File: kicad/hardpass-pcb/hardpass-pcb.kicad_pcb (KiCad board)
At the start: 2 copper layers, 80 x 65 mm, 59 parts, among them P1 Pi_Zero, P2 OLED_I2C, P3 Pi_Zero, SW1 1, SW10 C/UP, SW11 0/OK, SW12 OK/DN, SW2 2, SW3 3, SW4 4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

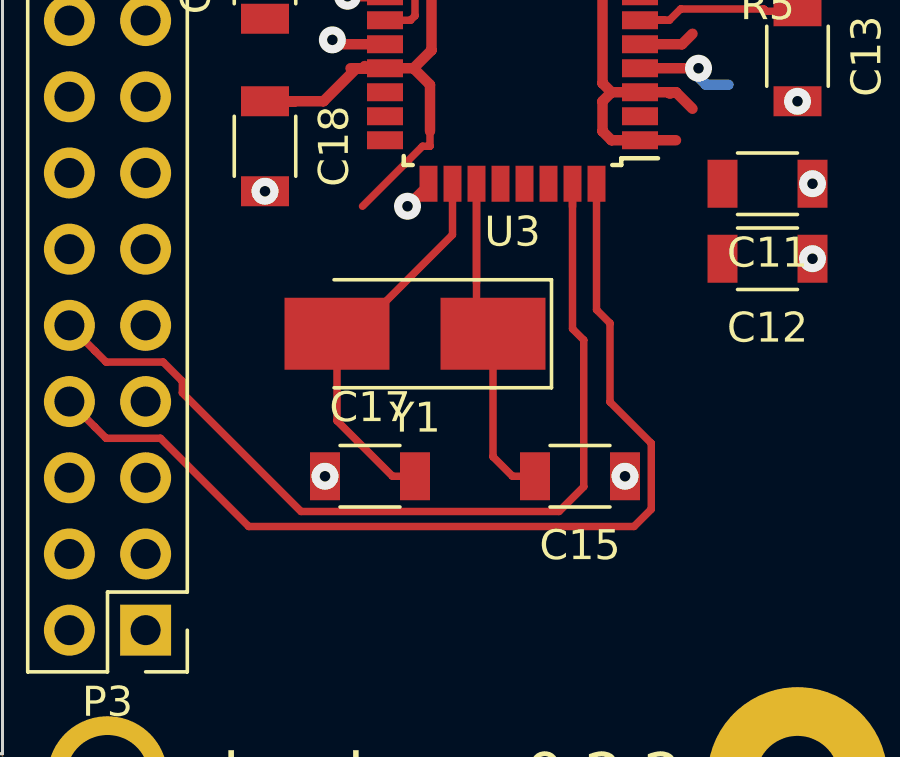
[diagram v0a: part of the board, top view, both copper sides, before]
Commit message: cleanup tracks around xtal
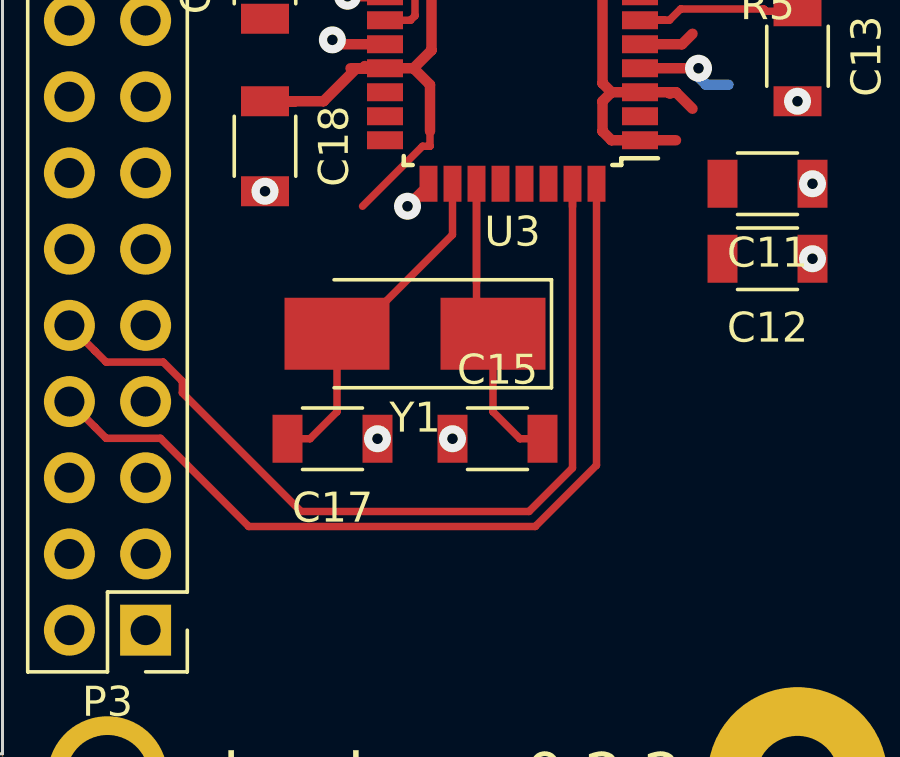
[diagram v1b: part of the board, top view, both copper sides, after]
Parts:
- moved C15 3.02 mm to (66.5, 50.2), turned to 0 degrees
- moved C17 1.77 mm to (61.0, 50.2), turned to 180 degrees
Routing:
- net CARD_RX: track 33.0 -> 29.5 mm
- net Net-(C17-Pad2): track 13.2 -> 11.5 mm
- net Net-(C15-Pad2): track 14.3 -> 13.2 mm
- net CARD_TX: track 31.3 -> 30.4 mm
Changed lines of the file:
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@@
     (links 167)
     (no_connects 8)
-    (area -0.050001 -0.050001 80.050001 65.050001)
+    (area -0.666014 -0.573 80.050001 65.655)
     (thickness 1.6)
     (drawings 26)
-    (tracks 724)
+    (tracks 718)
     (zones 0)
     (modules 59)
@@
   )
   (module Capacitors_SMD:C_1206 (layer F.Cu)
-    (at 69.25 51.5 180)
+    (at 66.5 50.25)
     (descr "Capacitor SMD 1206, reflow soldering, AVX (see smccp.pdf)")
     (tags "capacitor 1206")
     (attr smd)
-    (fp_text reference C15 (at 0 -2.3 180) (layer F.SilkS)
+    (fp_text reference C15 (at 0 -2.3) (layer F.SilkS)
       (effects (font (size 1 1) (thickness 0.15)))
     )
-    (fp_text value 22pF (at 0 2.3 180) (layer F.Fab)
+    (fp_text value 22pF (at 0 2.3) (layer F.Fab)
       (effects (font (size 1 1) (thickness 0.15)))
     )
@@
     (fp_line (start 1 -1.025) (end -1 -1.025) (layer F.SilkS) (width 0.12))
     (fp_line (start -1 1.025) (end 1 1.025) (layer F.SilkS) (width 0.12))
-    (pad 1 smd rect (at -1.5 0 180) (size 1 1.6) (layers F.Cu F.Paste F.Mask)
+    (pad 1 smd rect (at -1.5 0) (size 1 1.6) (layers F.Cu F.Paste F.Mask)
       (net 1 GND))
-    (pad 2 smd rect (at 1.5 0 180) (size 1 1.6) (layers F.Cu F.Paste F.Mask)
+    (pad 2 smd rect (at 1.5 0) (size 1 1.6) (layers F.Cu F.Paste F.Mask)
       (net 72 "Net-(C15-Pad2)"))
     (model Capacitors_SMD.3dshapes/C_1206.wrl
@@
   )
   (module Capacitors_SMD:C_1206 (layer F.Cu)
-    (at 62.25 51.5)
+    (at 61 50.25 180)
     (descr "Capacitor SMD 1206, reflow soldering, AVX (see smccp.pdf)")
     (tags "capacitor 1206")
     (attr smd)
-    (fp_text reference C17 (at 0 -2.3) (layer F.SilkS)
+    (fp_text reference C17 (at 0 -2.3 180) (layer F.SilkS)
       (effects (font (size 1 1) (thickness 0.15)))
     )
-    (fp_text value 22pF (at 0 2.3) (layer F.Fab)
+    (fp_text value 22pF (at 0 2.3 180) (layer F.Fab)
       (effects (font (size 1 1) (thickness 0.15)))
     )
@@
     (fp_line (start 1 -1.025) (end -1 -1.025) (layer F.SilkS) (width 0.12))
     (fp_line (start -1 1.025) (end 1 1.025) (layer F.SilkS) (width 0.12))
-    (pad 1 smd rect (at -1.5 0) (size 1 1.6) (layers F.Cu F.Paste F.Mask)
+    (pad 1 smd rect (at -1.5 0 180) (size 1 1.6) (layers F.Cu F.Paste F.Mask)
       (net 1 GND))
-    (pad 2 smd rect (at 1.5 0) (size 1 1.6) (layers F.Cu F.Paste F.Mask)
+    (pad 2 smd rect (at 1.5 0 180) (size 1 1.6) (layers F.Cu F.Paste F.Mask)
       (net 74 "Net-(C17-Pad2)"))
     (model Capacitors_SMD.3dshapes/C_1206.wrl
@@
   (via (at 71 32) (size 0.9) (drill 0.35) (layers F.Cu B.Cu) (net 1))
   (via (at 70.5 30.25) (size 0.9) (drill 0.35) (layers F.Cu B.Cu) (net 1))
-  (via (at 70.75 51.5) (size 0.9) (drill 0.35) (layers F.Cu B.Cu) (net 1))
-  (via (at 60.75 51.5) (size 0.9) (drill 0.35) (layers F.Cu B.Cu) (net 1))
+  (via (at 65 50.25) (size 0.9) (drill 0.35) (layers F.Cu B.Cu) (net 1))
+  (via (at 62.5 50.25) (size 0.9) (drill 0.35) (layers F.Cu B.Cu) (net 1))
   (via (at 73.2 37.9) (size 0.9) (drill 0.35) (layers F.Cu B.Cu) (net 1))
   (segment (start 62.75 37.1) (end 61.142188 37.1) (width 0.35) (layer F.Cu) (net 1))
@@
   (segment (start 75.45 36) (end 76.5 36) (width 0.25) (layer F.Cu) (net 71))
   (segment (start 72.1 36.3) (end 71.25 36.3) (width 0.25) (layer F.Cu) (net 71))
-  (segment (start 66.35 46.75) (end 66.35 50.85) (width 0.25) (layer F.Cu) (net 72))
-  (segment (start 66.35 50.85) (end 67 51.5) (width 0.25) (layer F.Cu) (net 72))
-  (segment (start 67 51.5) (end 67.75 51.5) (width 0.25) (layer F.Cu) (net 72))
+  (segment (start 66.35 46.75) (end 66.35 49.35) (width 0.25) (layer F.Cu) (net 72))
+  (segment (start 67.25 50.25) (end 68 50.25) (width 0.25) (layer F.Cu) (net 72))
+  (segment (start 66.35 49.35) (end 67.25 50.25) (width 0.25) (layer F.Cu) (net 72))
   (segment (start 65.8 41.75) (end 65.8 46.2) (width 0.25) (layer F.Cu) (net 72))
   (segment (start 65.8 46.2) (end 66.35 46.75) (width 0.25) (layer F.Cu) (net 72))
   (segment (start 65.8 41.75) (end 65.8 45.05) (width 0.25) (layer F.Cu) (net 72))
-  (segment (start 61.15 46.75) (end 61.15 49.65) (width 0.25) (layer F.Cu) (net 74))
-  (segment (start 61.15 49.65) (end 63 51.5) (width 0.25) (layer F.Cu) (net 74))
-  (segment (start 63 51.5) (end 63.75 51.5) (width 0.25) (layer F.Cu) (net 74))
+  (segment (start 61.15 46.75) (end 61.15 49.35) (width 0.25) (layer F.Cu) (net 74))
+  (segment (start 61.15 49.35) (end 60.25 50.25) (width 0.25) (layer F.Cu) (net 74))
+  (segment (start 60.25 50.25) (end 59.5 50.25) (width 0.25) (layer F.Cu) (net 74))
   (segment (start 65 41.75) (end 65 43.45) (width 0.25) (layer F.Cu) (net 74))
   (segment (start 61.7 46.75) (end 61.15 46.75) (width 0.25) (layer F.Cu) (net 74))
@@
   (segment (start 72.1 35.5) (end 71.25 35.5) (width 0.25) (layer F.Cu) (net 81))
   (segment (start 72.574999 35.375001) (end 72.224999 35.375001) (width 0.25) (layer F.Cu) (net 81))
-  (segment (start 69 41.75) (end 69 46.584998) (width 0.25) (layer F.Cu) (net 91))
-  (segment (start 69.375001 46.959999) (end 69.375001 51.850001) (width 0.25) (layer F.Cu) (net 91))
-  (segment (start 69 46.584998) (end 69.375001 46.959999) (width 0.25) (layer F.Cu) (net 91))
-  (segment (start 69.375001 51.850001) (end 68.550001 52.675001) (width 0.25) (layer F.Cu) (net 91))
-  (segment (start 68.550001 52.675001) (end 59.949999 52.675001) (width 0.25) (layer F.Cu) (net 91))
+  (segment (start 69 41.75) (end 69 51.225002) (width 0.25) (layer F.Cu) (net 91))
+  (segment (start 69 51.225002) (end 67.550001 52.675001) (width 0.25) (layer F.Cu) (net 91))
   (segment (start 59.949999 52.675001) (end 55.995001 48.720003) (width 0.25) (layer F.Cu) (net 91))
-  (segment (start 53.455001 47.695001) (end 53.079999 47.319999) (width 0.25) (layer F.Cu) (net 91))
+  (segment (start 67.550001 52.675001) (end 59.949999 52.675001) (width 0.25) (layer F.Cu) (net 91))
   (segment (start 55.995001 48.720003) (end 55.995001 48.332001) (width 0.25) (layer F.Cu) (net 91))
   (segment (start 55.995001 48.332001) (end 55.358001 47.695001) (width 0.25) (layer F.Cu) (net 91))
+  (segment (start 53.455001 47.695001) (end 53.079999 47.319999) (width 0.25) (layer F.Cu) (net 91))
   (segment (start 55.358001 47.695001) (end 53.455001 47.695001) (width 0.25) (layer F.Cu) (net 91))
   (segment (start 53.079999 47.319999) (end 52.23 46.47) (width 0.25) (layer F.Cu) (net 91))
   (segment (start 69 41.75) (end 69 42.525002) (width 0.25) (layer F.Cu) (net 91))
-  (segment (start 69.8 41.75) (end 69.8 45.95) (width 0.25) (layer F.Cu) (net 92))
-  (segment (start 71.625001 50.399999) (end 71.625001 52.600001) (width 0.25) (layer F.Cu) (net 92))
+  (segment (start 69.8 41.75) (end 69.8 51.132122) (width 0.25) (layer F.Cu) (net 92))
   (segment (start 58.208013 53.175011) (end 55.268003 50.235001) (width 0.25) (layer F.Cu) (net 92))
+  (segment (start 69.8 51.132122) (end 67.757111 53.175011) (width 0.25) (layer F.Cu) (net 92))
+  (segment (start 67.757111 53.175011) (end 58.208013 53.175011) (width 0.25) (layer F.Cu) (net 92))
   (segment (start 55.268003 50.235001) (end 53.455001 50.235001) (width 0.25) (layer F.Cu) (net 92))
-  (segment (start 69.8 45.95) (end 70.25 46.4) (width 0.25) (layer F.Cu) (net 92))
   (segment (start 53.455001 50.235001) (end 53.079999 49.859999) (width 0.25) (layer F.Cu) (net 92))
-  (segment (start 70.25 46.4) (end 70.25 49.024998) (width 0.25) (layer F.Cu) (net 92))
-  (segment (start 70.25 49.024998) (end 71.625001 50.399999) (width 0.25) (layer F.Cu) (net 92))
-  (segment (start 71.625001 52.600001) (end 71.049991 53.175011) (width 0.25) (layer F.Cu) (net 92))
-  (segment (start 71.049991 53.175011) (end 58.208013 53.175011) (width 0.25) (layer F.Cu) (net 92))
   (segment (start 53.079999 49.859999) (end 52.23 49.01) (width 0.25) (layer F.Cu) (net 92))
   (segment (start 70.45 27.25) (end 70.45 27.65) (width 0.25) (layer F.Cu) (net 121))

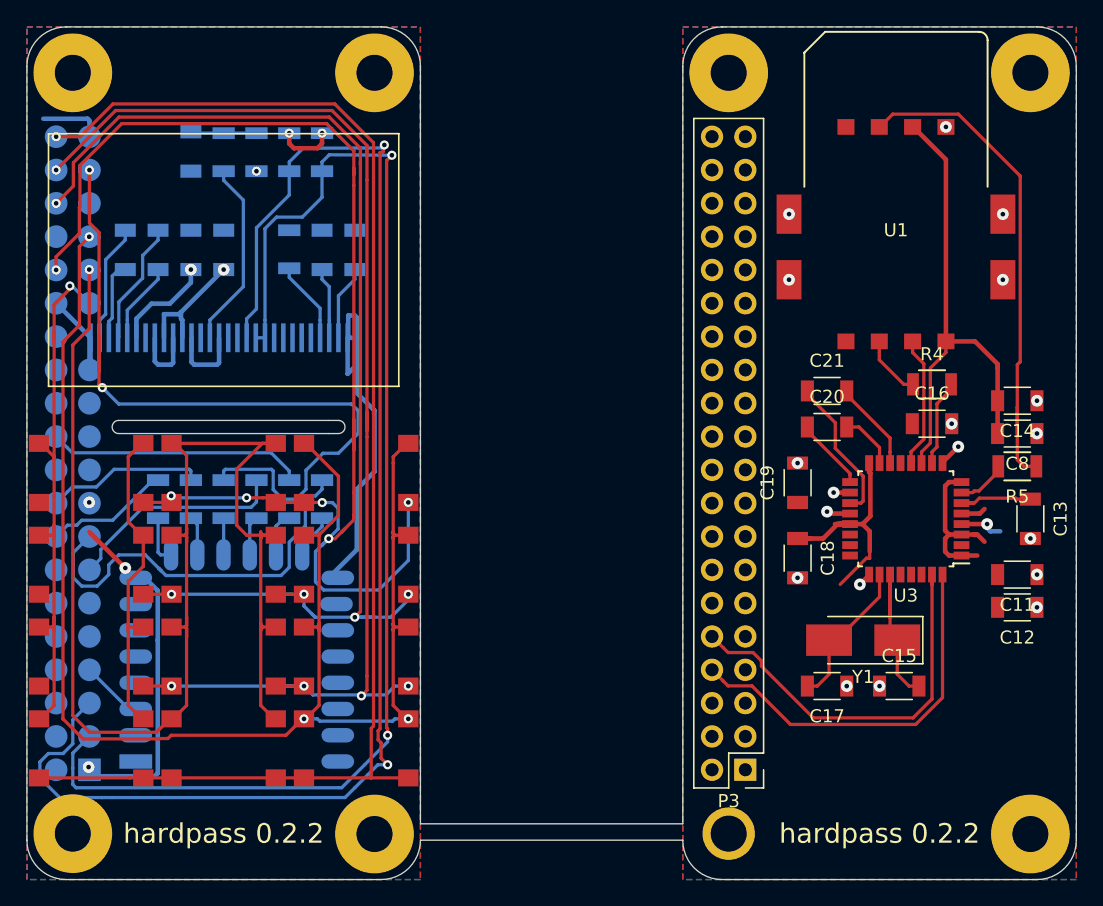
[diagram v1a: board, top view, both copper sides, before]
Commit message: fixed multiple things, add gnu logo
fixed:
 * mounting holes now non plated
 * fixed a few wires here and there
 * added a gnu/gpl logo for testing graphics
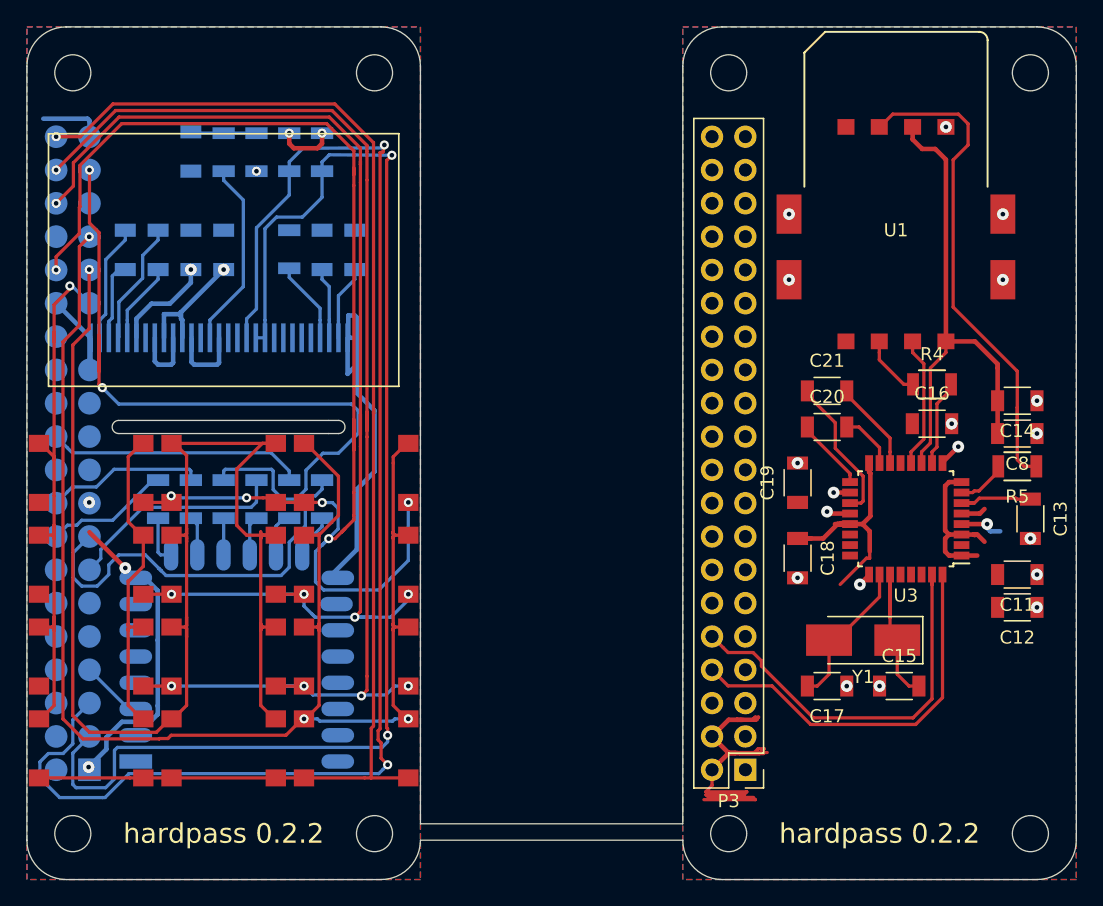
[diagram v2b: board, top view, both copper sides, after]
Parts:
- removed the REF** at (76.5, 61.5)
- removed the REF** at (76.5, 3.50)
- removed the REF** at (53.5, 3.50)
- removed the REF** at (53.5, 61.5)
- removed the REF** at (26.5, 61.5)
- removed the REF** at (3.50, 61.5)
- removed the REF** at (26.5, 3.50)
- removed the REF** at (3.50, 3.50)
- added ?: , RPi_Hat:RPi_Hat_Mounting_Hole, F.Cu at (53.5, 61.5)
- added ?: , RPi_Hat:RPi_Hat_Mounting_Hole, F.Cu at (76.5, 61.5)
- added ?: , RPi_Hat:RPi_Hat_Mounting_Hole, F.Cu at (76.5, 3.50)
- added ?: , RPi_Hat:RPi_Hat_Mounting_Hole, F.Cu at (53.5, 3.50)
- added ?: , RPi_Hat:RPi_Hat_Mounting_Hole, F.Cu at (26.5, 3.50)
- added ?: , RPi_Hat:RPi_Hat_Mounting_Hole, F.Cu at (26.5, 61.5)
- added ?: , RPi_Hat:RPi_Hat_Mounting_Hole, F.Cu at (3.50, 61.5)
- added ?: , RPi_Hat:RPi_Hat_Mounting_Hole, F.Cu at (3.50, 3.50)
- added REF**: Symbol_GNU-Logo_MaskTop, hardpass:Symbol_GNU-Logo_MaskTop, B.Cu at (65.0, 21.2)
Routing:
- net +5V: track 33.4 -> 73.8 mm
- net +3V3: track 49.4 -> 46.8 mm
- net OLED_SDA: track 97.4 -> 98.6 mm
- net Net-(R5-Pad1): track 38.5 -> 39.2 mm
- net Net-(C14-Pad2): track 37.4 -> 38.0 mm

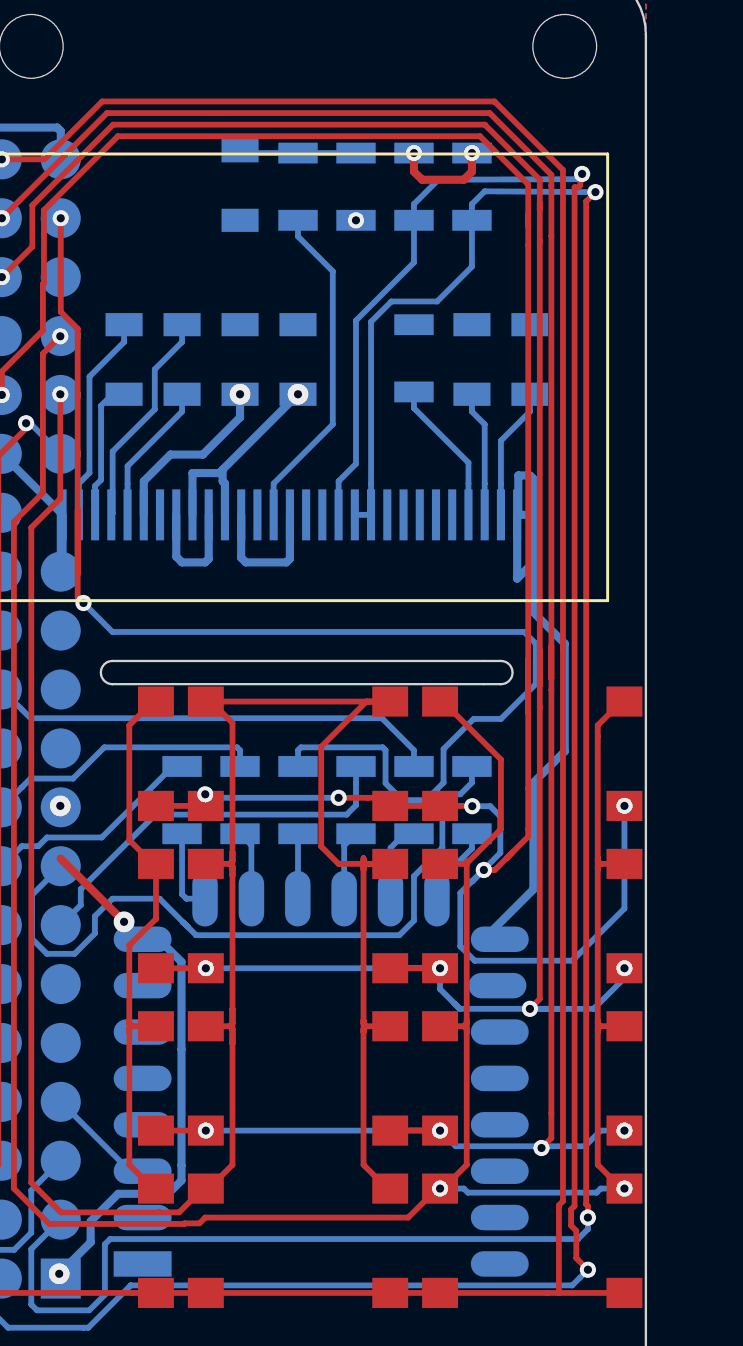
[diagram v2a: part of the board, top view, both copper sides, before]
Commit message: reset circuit works; cleanup on it
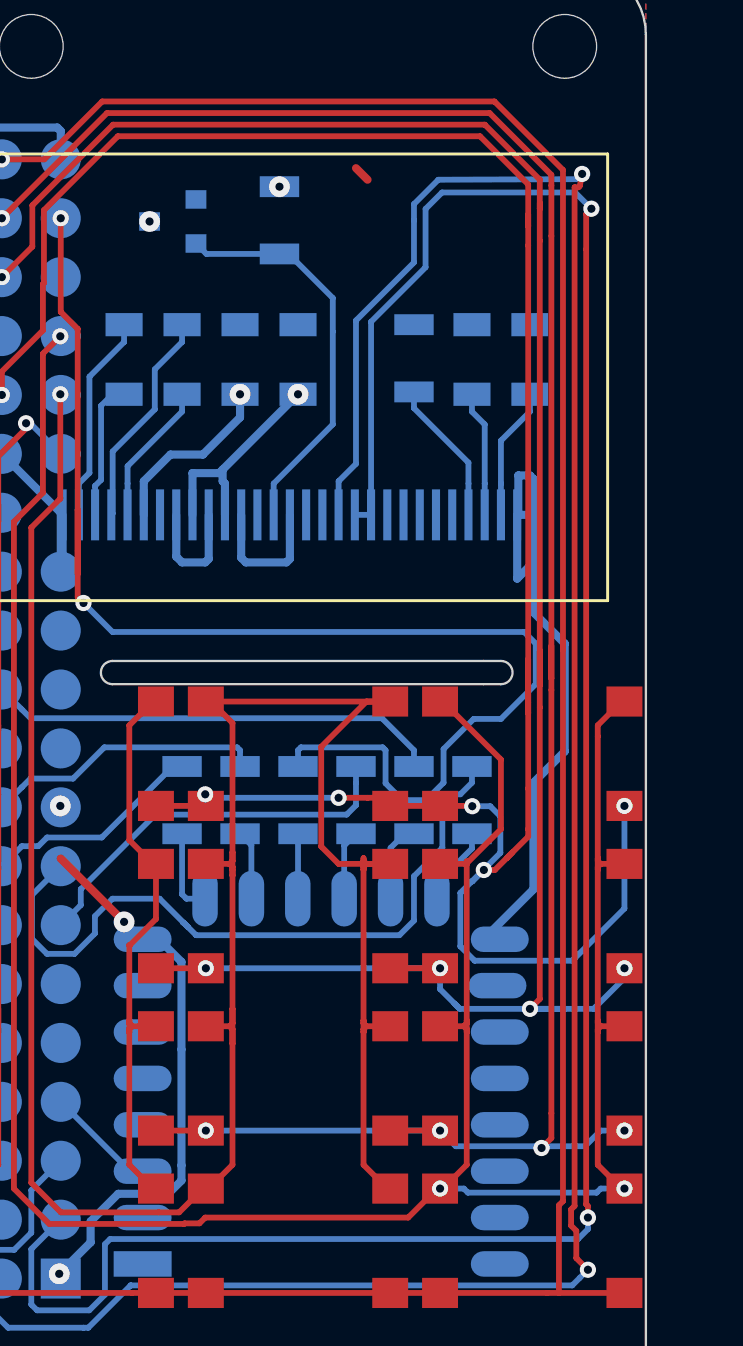
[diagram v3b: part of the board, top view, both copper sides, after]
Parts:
- removed C7: 0.1µF, Capacitors_SMD:C_1206
- removed R10, R11: 10k, Resistors_SMD:R_1206
- removed R3: 100k, Resistors_SMD:R_1206
- added IC1: APX803, TO_SOT_Packages_SMD:SOT-23, B.Cu at (9.60, 11.1)
- C1, C2, C5, C6: value 1µF -> 2.2µF
- C3: value 2.2µF -> 10µF
- C4: value 4.7µF -> 2.2µF
- R2: value 100k -> 10k
- moved R2 3.60 mm to (14.2, 11.0)
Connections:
- P2 pad 14: Net-(P2-Pad14) -> OLED_RST
- R2 pad 1: Net-(C7-Pad1) -> +3V3
- R2 pad 2: +3V3 -> OLED_RST
- U1 pad : GND -> (no net)
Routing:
- net OLED_RST: track 0.00 -> 17.3 mm
- net Net-(P2-Pad14): track 14.4 -> 0.00 mm
- net Net-(C7-Pad1): track 5.04 -> 0.00 mm
- net +3V3: track 46.8 -> 43.1 mm, vias 8 -> 7
- net OLED_SDA: track 98.6 -> 97.7 mm
- net GND: vias 20 -> 16
- net (no net): vias 0 -> 4
